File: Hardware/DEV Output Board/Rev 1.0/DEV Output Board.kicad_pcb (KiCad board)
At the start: 2 copper layers, 100 x 100 mm, 14 parts, among them J1 SPEAKER, J2 SERIAL, U1 Waveshare 2.4in LCD Header, U2 Teensy4.0, U3 Waveshare 2.4in LCD

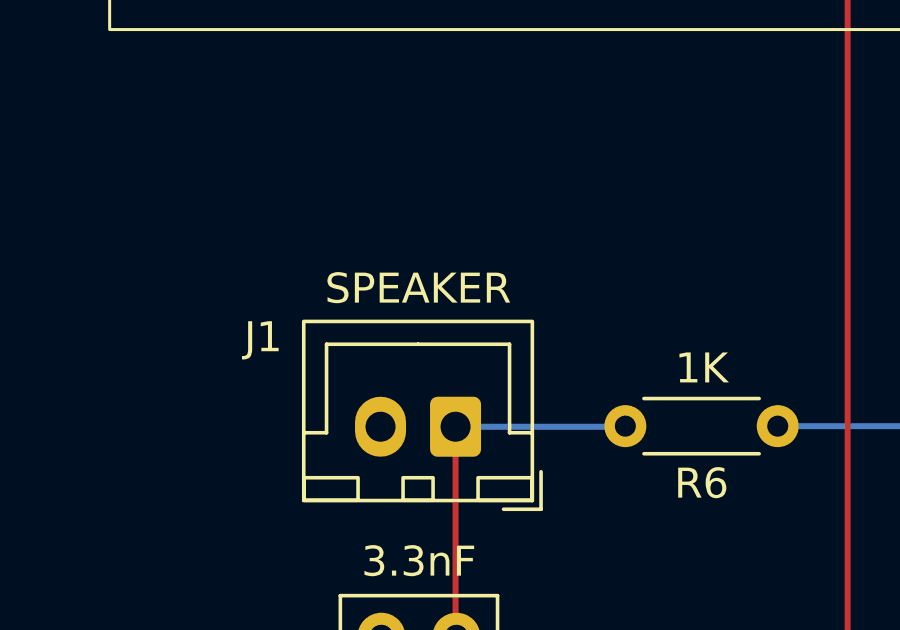
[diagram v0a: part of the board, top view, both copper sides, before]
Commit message: Update Dev Output Board silkscreen
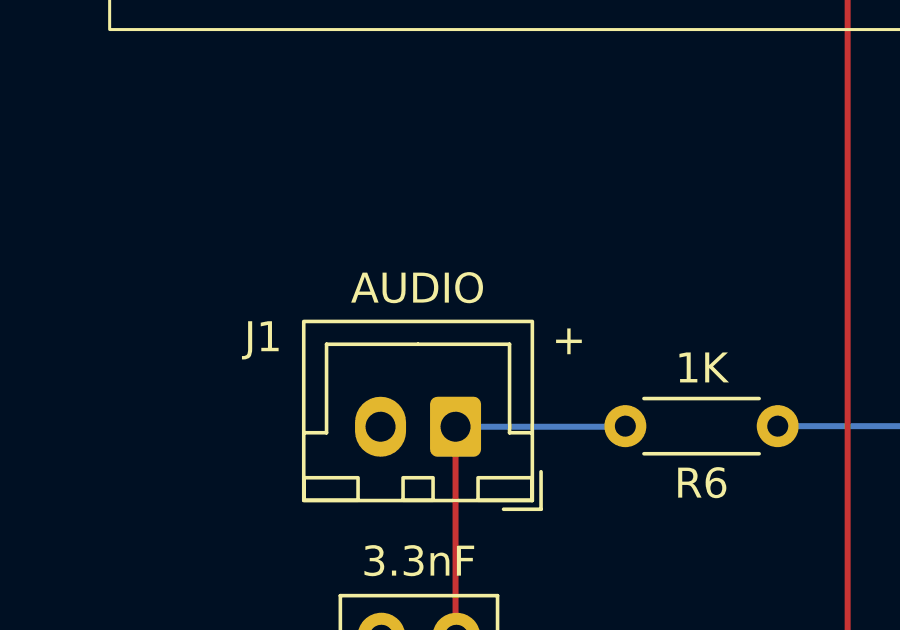
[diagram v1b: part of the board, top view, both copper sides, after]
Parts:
- J1: value SPEAKER -> AUDIO
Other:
- board text added: "+"
